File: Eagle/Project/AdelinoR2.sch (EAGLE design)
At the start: 68 parts, among them J1 DC-044-A, J2 YELLOW-8P-2.54, J3 YELLOW-6P-2.54, J4 YELLOW-8P-2.54, J5 YELLOW-8P-2.54, J6 4P-2.0, J7 YELLOW-2X3P-2.54, J8 4P-2.0, Q1 NCE3407A, Q2 CJ2305, SW1 TS-1101F, U1 MP1496DJ-SOT23-8, U2 CJT1117-3.3-SOT223, U3 ESP-12F / OPL: 317060163 / SM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, U4 ATMEGA32U4-MUR-QFN44, U5 74VHC125MTCX-TSSOP14, X1 306010049_XTAL_16MHZ-3225_4P

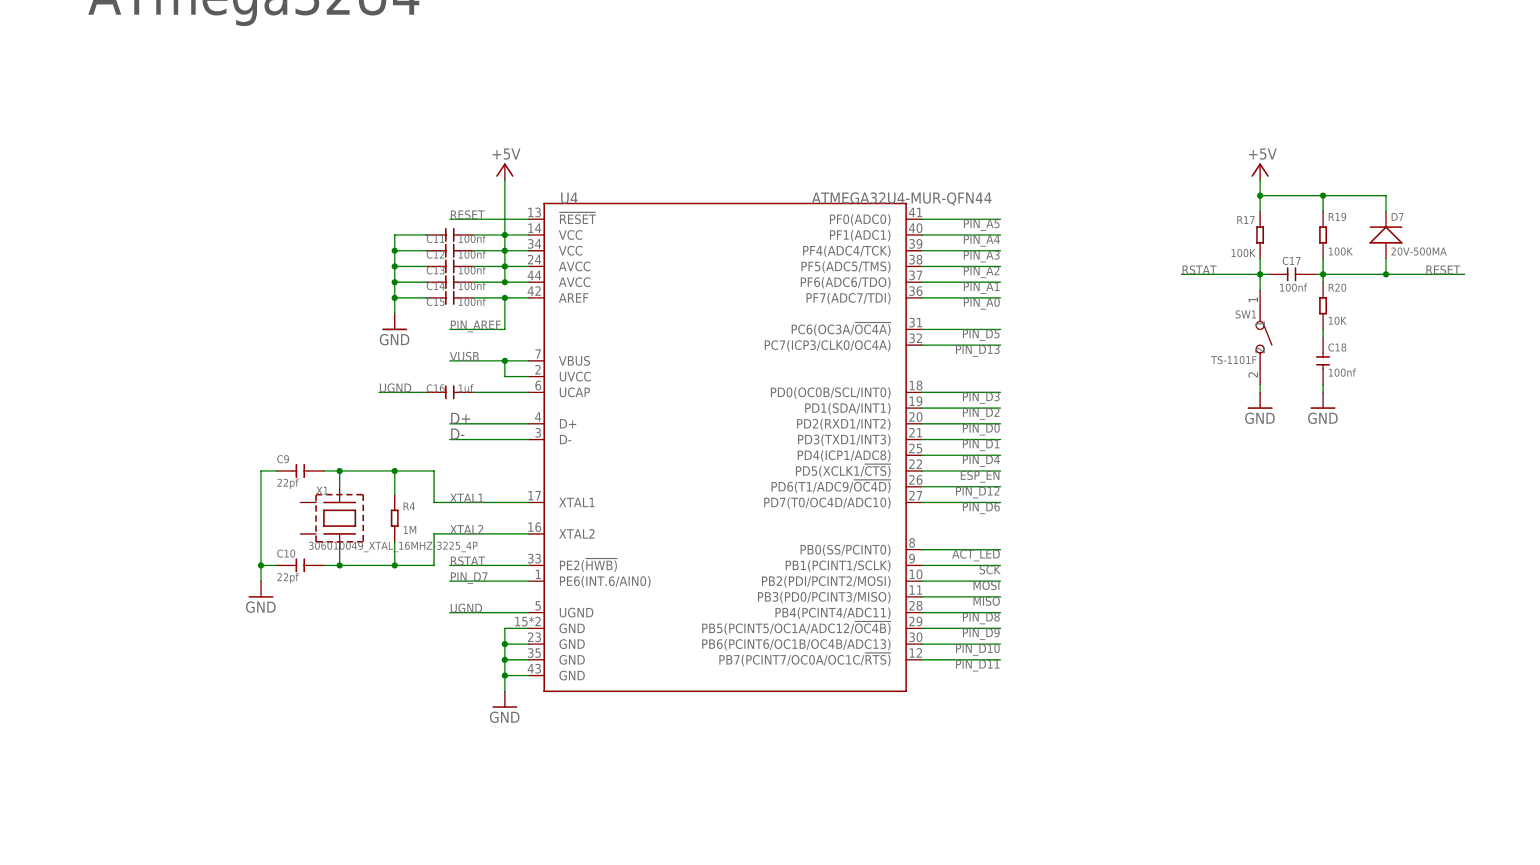
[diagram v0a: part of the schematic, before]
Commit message: Add alternative TQFP44 socket alongside QFN44.
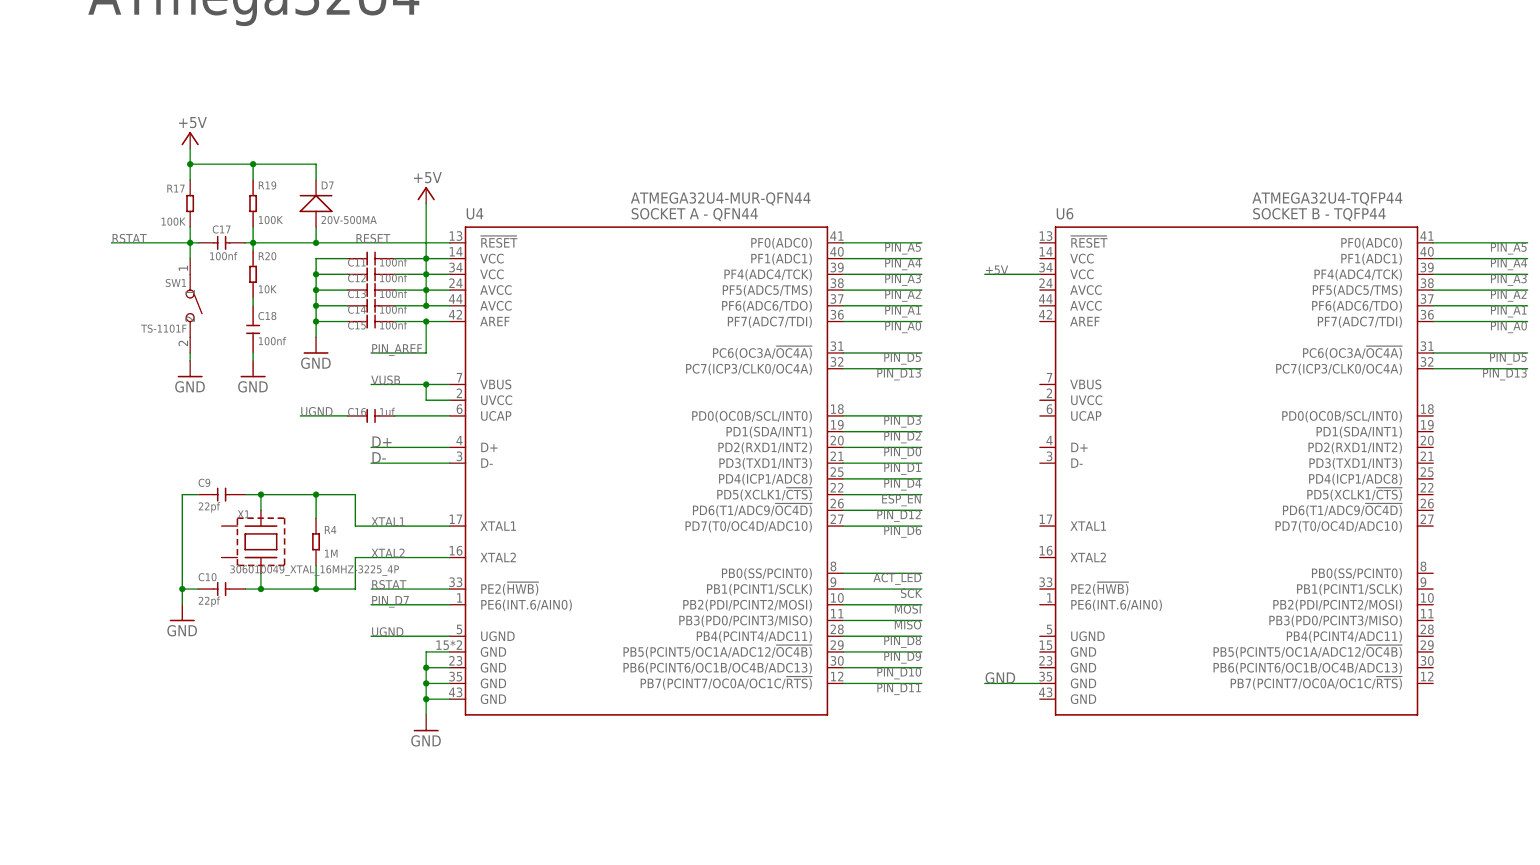
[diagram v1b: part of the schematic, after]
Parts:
- added U6: ATMEGA32U4-TQFP44, Seeed-IC:MCU-ATMEGA32U4-AU(TQFP44)
- U4: DESC (none) -> SOCKET A - QFN44
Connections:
- net +5V: now also U6.VCC@2
- net GND: now also U6.GND@3
- net PIN_A0: now also U6.PF7(ADC7/TDI)
- net PIN_A1: now also U6.PF6(ADC6/TDO)
- net PIN_A2: now also U6.PF5(ADC5/TMS)
- net PIN_A3: now also U6.PF4(ADC4/TCK)
- net PIN_A4: now also U6.PF1(ADC1)
- net PIN_A5: now also U6.PF0(ADC0)
- net PIN_D13: now also U6.PC7(ICP3/CLK0/OC4A)
- net PIN_D5: now also U6.PC6(OC3A/!OC4A)
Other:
- moved on the sheet: C10, C11, C12, C13, C14, C15, C16, C17, C18, C9, D7, R17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

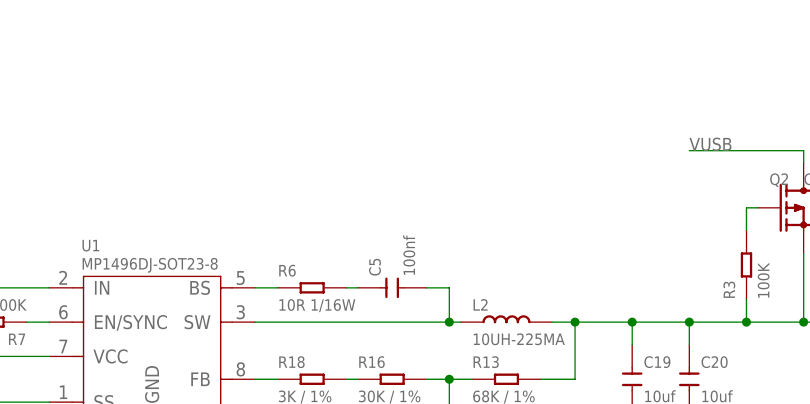
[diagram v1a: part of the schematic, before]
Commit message: Getting proper double-socket pairing; minor tweaks.
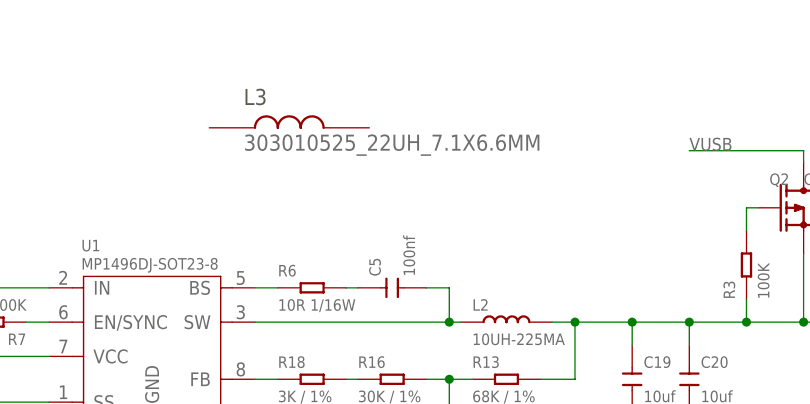
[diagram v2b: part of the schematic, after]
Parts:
- added L3: 303010525_22UH_7.1X6.6MM, Seeed-OPL-2017-01-Inductor-Akita:303010525_22UH_7.1X6.6MM
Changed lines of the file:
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@@
 <setting verticaltext="up"/>
 </settings>
-<grid distance="0.05" unitdist="inch" unit="inch" style="lines" multiple="1" display="no" altdistance="0.01" altunitdist="inch" altunit="inch"/>
+<grid distance="0.1" unitdist="inch" unit="inch" style="lines" multiple="1" display="no" altdistance="0.01" altunitdist="inch" altunit="inch"/>
 <layers>
 <layer number="1" name="Top" color="4" fill="1" visible="no" active="no"/>
@@
 <attribute name="DESC" value="SOCKET B - TQFP44"/>
 </part>
+<part name="L3" library="Seeed-OPL-2017-01-Inductor-Akita" deviceset="303010525_22UH_7.1X6.6MM" device=""/>
 </parts>
 <sheets>
@@
 <attribute name="DESC" x="201.93" y="133.35" size="1.778" layer="96"/>
 </instance>
+<instance part="L3" gate="G$1" x="-137.16" y="165.1" smashed="yes">
+<attribute name="NAME" x="-142.24" y="167.64" size="1.778" layer="97"/>
+<attribute name="VALUE" x="-142.24" y="162.56" size="1.778" layer="96"/>
+</instance>
 </instances>

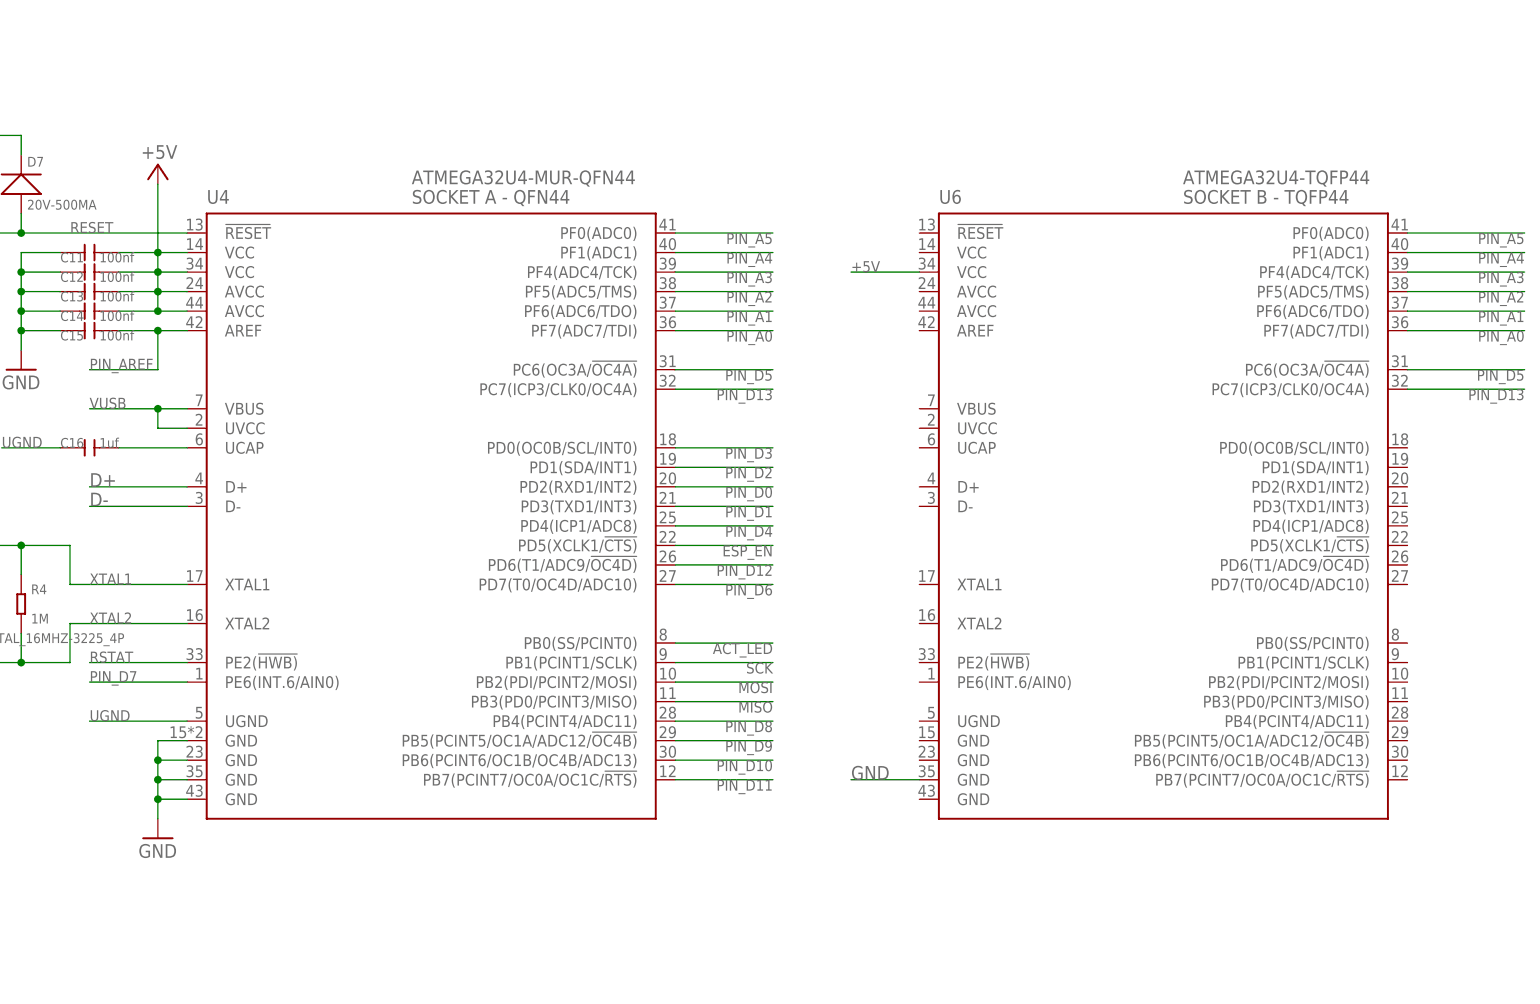
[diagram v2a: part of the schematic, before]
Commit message: Double socket TQFP44+QFN44 finished.
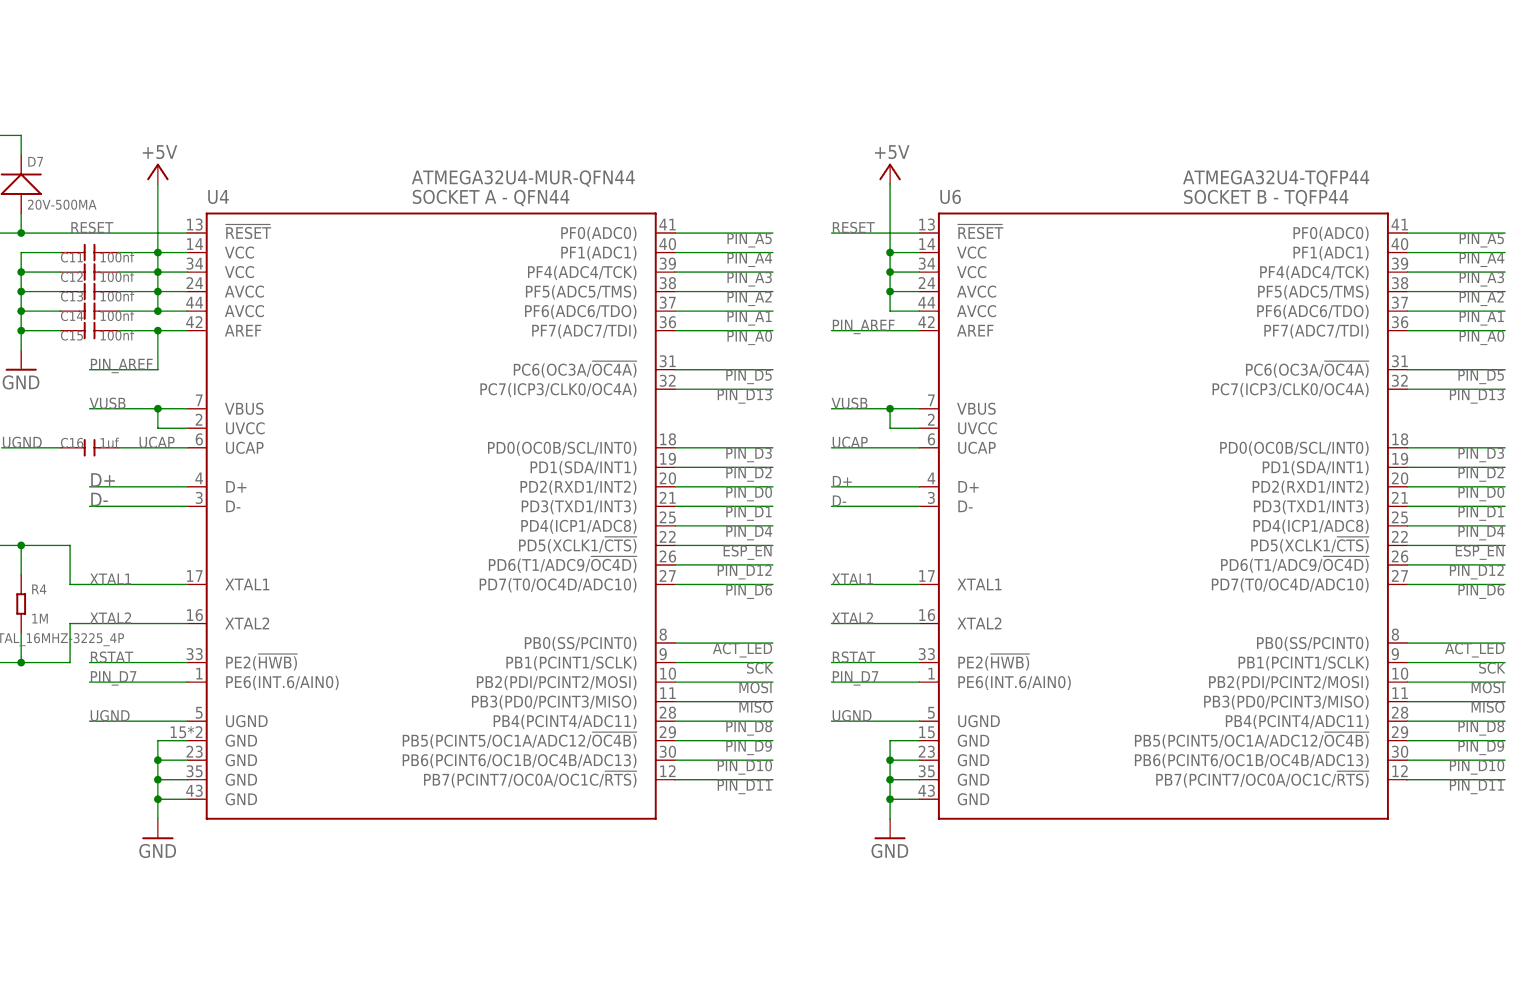
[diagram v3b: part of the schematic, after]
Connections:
- removed net N$7: C16.2, U4.UCAP
- new net UCAP: C16.2, U4.UCAP, U6.UCAP
- net +5V: now also U6.AVCC@1, U6.AVCC@2, U6.VCC@1
- net ACT_LED: now also U6.PB0(SS/PCINT0)
- net D+: now also U6.D+
- net D-: now also U6.D-
- net ESP_EN: now also U6.PD5(XCLK1/!CTS)
- net GND: now also U6.GND@1, U6.GND@2, U6.GND@4
- net MISO: now also U6.PB3(PD0/PCINT3/MISO)
- net MOSI: now also U6.PB2(PDI/PCINT2/MOSI)
- net PIN_AREF: now also U6.AREF
- net PIN_D0: now also U6.PD2(RXD1/INT2)
- net PIN_D1: now also U6.PD3(TXD1/INT3)
- net PIN_D10: now also U6.PB6(PCINT6/OC1B/OC4B/ADC13)
- net PIN_D11: now also U6.PB7(PCINT7/OC0A/OC1C/!RTS)
- net PIN_D12: now also U6.PD6(T1/ADC9/!OC4D)
- net PIN_D2: now also U6.PD1(SDA/INT1)
- net PIN_D3: now also U6.PD0(OC0B/SCL/INT0)
- net PIN_D4: now also U6.PD4(ICP1/ADC8)
- net PIN_D6: now also U6.PD7(T0/OC4D/ADC10)
- net PIN_D7: now also U6.PE6(INT.6/AIN0)
- net PIN_D8: now also U6.PB4(PCINT4/ADC11)
- net PIN_D9: now also U6.PB5(PCINT5/OC1A/ADC12/!OC4B)
- net RESET: now also U6.!RESET
- net RSTAT: now also U6.PE2(!HWB)
- net SCK: now also U6.PB1(PCINT1/SCLK)
- net UGND: now also U6.UGND
- net VUSB: now also U6.UVCC, U6.VBUS
- net XTAL1: now also U6.XTAL1
- net XTAL2: now also U6.XTAL2
